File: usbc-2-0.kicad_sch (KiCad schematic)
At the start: 8 parts, among them J201 USB_C_Receptacle_USB2.0

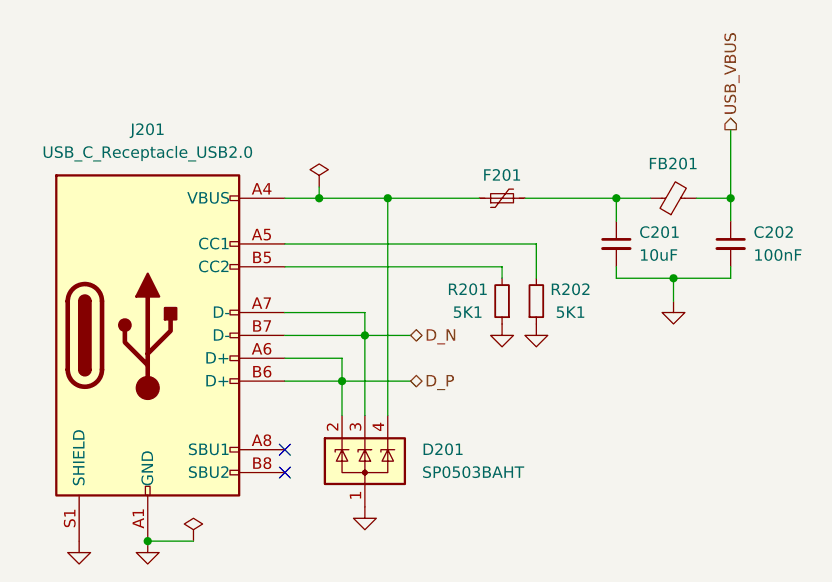
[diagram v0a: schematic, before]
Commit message: update schematic
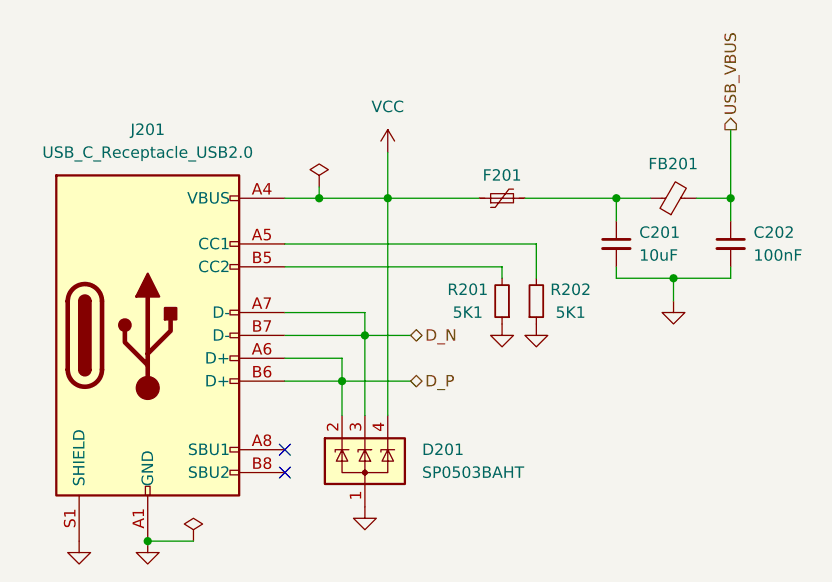
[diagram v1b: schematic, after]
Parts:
- J201: footprint User Custom Footprint:USB_C_Receptable_918-418K2023S40001 -> User_Footprint:USB_C_Receptable_918-418K2023S40001
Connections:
- net VCC: now reaches D201.4 (K), F201.1, J201.A4 (VBUS), J201.A9 (VBUS), J201.B4 (VBUS), J201.B9 (VBUS)
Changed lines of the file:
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@@
+    (stroke (width 0) (type default))
+  )
+  (wire (pts (xy 77.47 33.02) (xy 77.47 38.1))
     (stroke (width 0) (type default))
   )
@@
   (symbol (lib_id "power:GND") (at 90.17 52.07 0) (unit 1)
     (in_bom yes) (on_board yes) (dnp no) (fields_autoplaced)
-    (property "Reference" "#PWR0202" (at 90.17 58.42 0)
+    (property "Reference" "#PWR0203" (at 90.17 58.42 0)
       (effects (font (size 1.27 1.27)) hide)
     )
@@
       (project "wled-esp32-control-board"
         (path "/39949f26-7b4e-4f4c-975a-4ef261468b2a/06531422-46ec-4b81-b2a2-21a1afed1c45"
-          (reference "#PWR0202") (unit 1)
+          (reference "#PWR0203") (unit 1)
         )
       )
@@
   (symbol (lib_id "power:GND") (at 43.18 76.2 0) (unit 1)
     (in_bom yes) (on_board yes) (dnp no) (fields_autoplaced)
-    (property "Reference" "#PWR0205" (at 43.18 82.55 0)
+    (property "Reference" "#PWR0206" (at 43.18 82.55 0)
       (effects (font (size 1.27 1.27)) hide)
     )
@@
       (project "wled-esp32-control-board"
         (path "/39949f26-7b4e-4f4c-975a-4ef261468b2a/06531422-46ec-4b81-b2a2-21a1afed1c45"
+          (reference "#PWR0206") (unit 1)
+        )
+      )
+      (project "arudino-clone"
+        (path "/7b2b1845-59f7-4bfa-9efc-3639d821cf70"
+          (reference "#PWR?") (unit 1)
+        )
+        (path "/7b2b1845-59f7-4bfa-9efc-3639d821cf70/42f81444-0f87-48cc-869b-f9c5fa4e11c4"
           (reference "#PWR0205") (unit 1)
         )
       )
-      (project "arudino-clone"
-        (path "/7b2b1845-59f7-4bfa-9efc-3639d821cf70"
-          (reference "#PWR?") (unit 1)
-        )
-        (path "/7b2b1845-59f7-4bfa-9efc-3639d821cf70/42f81444-0f87-48cc-869b-f9c5fa4e11c4"
-          (reference "#PWR0205") (unit 1)
-        )
-      )
     )
   )
@@
       (effects (font (size 1.27 1.27)))
     )
-    (property "Footprint" "User Custom Footprint:USB_C_Receptable_918-418K2023S40001" (at 54.61 53.34 0)
+    (property "Footprint" "User_Footprint:USB_C_Receptable_918-418K2023S40001" (at 54.61 53.34 0)
       (effects (font (size 1.27 1.27)) hide)
     )
@@
     )
   )
+  (symbol (lib_id "power:VCC") (at 77.47 33.02 0) (unit 1)
+    (in_bom yes) (on_board yes) (dnp no) (fields_autoplaced)
+    (property "Reference" "#PWR0201" (at 77.47 36.83 0)
+      (effects (font (size 1.27 1.27)) hide)
+    )
+    (property "Value" "VCC" (at 77.47 27.94 0)
+      (effects (font (size 1.27 1.27)))
+    )
+    (property "Footprint" "" (at 77.47 33.02 0)
+      (effects (font (size 1.27 1.27)) hide)
+    )
+    (property "Datasheet" "" (at 77.47 33.02 0)
+      (effects (font (size 1.27 1.27)) hide)
+    )
+    (pin "1")
+    (instances
+      (project "wled-esp32-control-board"
+        (path "/39949f26-7b4e-4f4c-975a-4ef261468b2a/06531422-46ec-4b81-b2a2-21a1afed1c45"
+          (reference "#PWR0201") (unit 1)
+        )
+      )
+    )
+  )
   (symbol (lib_id "Device:R_Small") (at 90.17 49.53 180) (unit 1)
     (in_bom yes) (on_board yes) (dnp no)
@@
   (symbol (lib_id "power:GND") (at 50.8 76.2 0) (unit 1)
     (in_bom yes) (on_board yes) (dnp no) (fields_autoplaced)
-    (property "Reference" "#PWR0206" (at 50.8 82.55 0)
+    (property "Reference" "#PWR0207" (at 50.8 82.55 0)
       (effects (font (size 1.27 1.27)) hide)
     )
@@
       (project "wled-esp32-control-board"
         (path "/39949f26-7b4e-4f4c-975a-4ef261468b2a/06531422-46ec-4b81-b2a2-21a1afed1c45"
+          (reference "#PWR0207") (unit 1)
+        )
+      )
+      (project "arudino-clone"
+        (path "/7b2b1845-59f7-4bfa-9efc-3639d821cf70"
+          (reference "#PWR?") (unit 1)
+        )
+        (path "/7b2b1845-59f7-4bfa-9efc-3639d821cf70/42f81444-0f87-48cc-869b-f9c5fa4e11c4"
           (reference "#PWR0206") (unit 1)
         )
       )
-      (project "arudino-clone"
-        (path "/7b2b1845-59f7-4bfa-9efc-3639d821cf70"
-          (reference "#PWR?") (unit 1)
-        )
-        (path "/7b2b1845-59f7-4bfa-9efc-3639d821cf70/42f81444-0f87-48cc-869b-f9c5fa4e11c4"
-          (reference "#PWR0206") (unit 1)
-        )
-      )
     )
   )
   (symbol (lib_id "power:GND") (at 93.98 52.07 0) (unit 1)
     (in_bom yes) (on_board yes) (dnp no) (fields_autoplaced)
-    (property "Reference" "#PWR0203" (at 93.98 58.42 0)
+    (property "Reference" "#PWR0204" (at 93.98 58.42 0)
       (effects (font (size 1.27 1.27)) hide)
     )
@@
       (project "wled-esp32-control-board"
         (path "/39949f26-7b4e-4f4c-975a-4ef261468b2a/06531422-46ec-4b81-b2a2-21a1afed1c45"
-          (reference "#PWR0203") (unit 1)
+          (reference "#PWR0204") (unit 1)
         )
       )
@@
   (symbol (lib_id "power:GND") (at 74.93 72.39 0) (unit 1)
     (in_bom yes) (on_board yes) (dnp no) (fields_autoplaced)
-    (property "Reference" "#PWR0204" (at 74.93 78.74 0)
+    (property "Reference" "#PWR0205" (at 74.93 78.74 0)
       (effects (font (size 1.27 1.27)) hide)
     )
@@
       (project "wled-esp32-control-board"
         (path "/39949f26-7b4e-4f4c-975a-4ef261468b2a/06531422-46ec-4b81-b2a2-21a1afed1c45"
+          (reference "#PWR0205") (unit 1)
+        )
+      )
+      (project "arudino-clone"
+        (path "/7b2b1845-59f7-4bfa-9efc-3639d821cf70"
+          (reference "#PWR?") (unit 1)
+        )
+        (path "/7b2b1845-59f7-4bfa-9efc-3639d821cf70/42f81444-0f87-48cc-869b-f9c5fa4e11c4"
           (reference "#PWR0204") (unit 1)
         )
       )
-      (project "arudino-clone"
-        (path "/7b2b1845-59f7-4bfa-9efc-3639d821cf70"
-          (reference "#PWR?") (unit 1)
-        )
-        (path "/7b2b1845-59f7-4bfa-9efc-3639d821cf70/42f81444-0f87-48cc-869b-f9c5fa4e11c4"
-          (reference "#PWR0204") (unit 1)
-        )
-      )
     )
   )
@@
   (symbol (lib_id "power:GND") (at 109.22 49.53 0) (unit 1)
     (in_bom yes) (on_board yes) (dnp no) (fields_autoplaced)
-    (property "Reference" "#PWR0201" (at 109.22 55.88 0)
+    (property "Reference" "#PWR0202" (at 109.22 55.88 0)
       (effects (font (size 1.27 1.27)) hide)
     )
@@
       (project "wled-esp32-control-board"
         (path "/39949f26-7b4e-4f4c-975a-4ef261468b2a/06531422-46ec-4b81-b2a2-21a1afed1c45"
-          (reference "#PWR0201") (unit 1)
-        )
-      )
+          (reference "#PWR0202") (unit 1)
+        )
+      )

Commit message: update parts
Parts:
- J201: Mouser (none) -> 523-12402012E212A
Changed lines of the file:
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@@
+      (effects (font (size 1.27 1.27)) hide)
+    )
+    (property "Mouser" "523-12402012E212A" (at 50.8 53.34 0)
       (effects (font (size 1.27 1.27)) hide)
     )

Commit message: add mouser part numbers
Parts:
- C201: Mouser (none) -> 581-0805ZD106K
- C202: Mouser (none) -> 581-06035C104KAT2A
- D201: Mouser (none) -> 576-SP0503BAHTG
- F201: Mouser (none) -> 576-0603L200SL-VYR
- FB201: Mouser (none) -> 810-MPZ2012S101AT000
- R201, R202: Mouser (none) -> 603-RC0603FR-075K1L
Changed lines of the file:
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@@
+      (effects (font (size 1.27 1.27)) hide)
+    )
+    (property "Mouser" "576-SP0503BAHTG" (at 74.93 67.31 0)
       (effects (font (size 1.27 1.27)) hide)
     )
@@
       (effects (font (size 1.27 1.27)) hide)
     )
+    (property "Mouser" "581-06035C104KAT2A" (at 115.57 43.18 0)
+      (effects (font (size 1.27 1.27)) hide)
+    )
     (pin "1")
     (pin "2")
@@
     )
     (property "LCSC" "C74487" (at 109.22 38.1 0)
+      (effects (font (size 1.27 1.27)) hide)
+    )
+    (property "Mouser" "810-MPZ2012S101AT000" (at 109.22 38.1 0)
       (effects (font (size 1.27 1.27)) hide)
     )
@@
       (effects (font (size 1.27 1.27)) hide)
     )
+    (property "Mouser" "603-RC0603FR-075K1L" (at 90.17 49.53 0)
+      (effects (font (size 1.27 1.27)) hide)
+    )
     (pin "1")
     (pin "2")
@@
     )
     (property "LCSC" "C23186" (at 93.98 49.53 0)
+      (effects (font (size 1.27 1.27)) hide)
+    )
+    (property "Mouser" "603-RC0603FR-075K1L" (at 93.98 49.53 0)
       (effects (font (size 1.27 1.27)) hide)
     )
@@
       (effects (font (size 1.27 1.27)) hide)
     )
+    (property "Mouser" "581-0805ZD106K" (at 102.87 43.18 0)
+      (effects (font (size 1.27 1.27)) hide)
+    )
     (pin "1")
     (pin "2")
@@
       (effects (font (size 1.27 1.27)) hide)
     )
+    (property "Mouser" "576-0603L200SL-VYR" (at 90.17 38.1 0)
+      (effects (font (size 1.27 1.27)) hide)
+    )

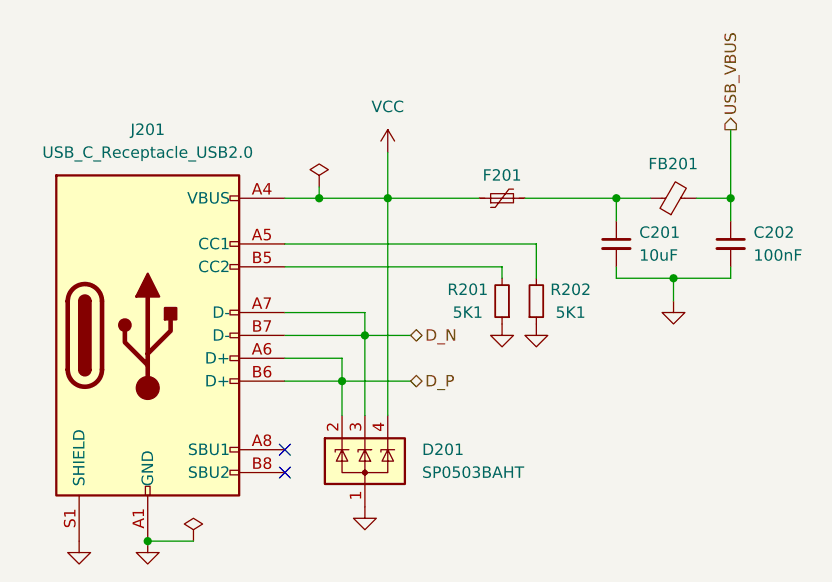
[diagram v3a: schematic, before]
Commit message: update design to replace CP2102 and LDO
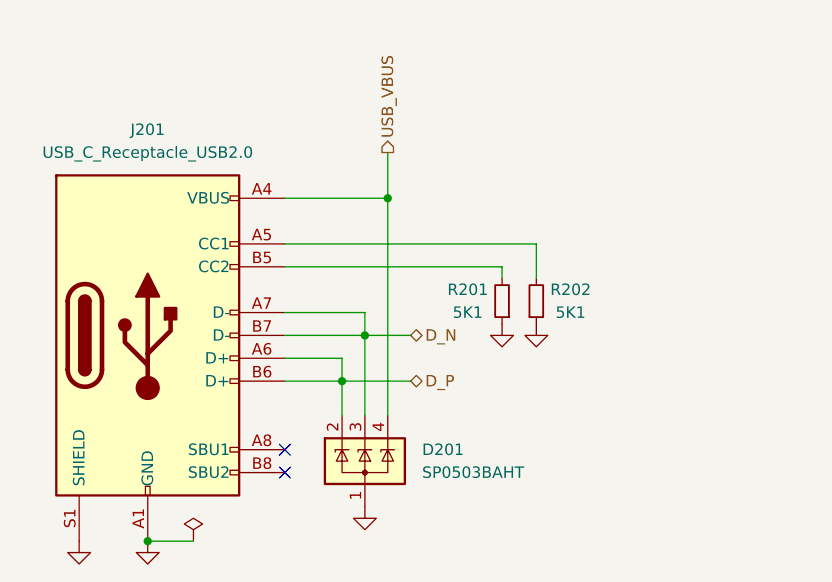
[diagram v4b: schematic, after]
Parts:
- removed C201: 10uF, Capacitor_SMD:C_0805_2012Metric, symbol Device:C_Small
- removed C202: 100nF, Capacitor_SMD:C_0603_1608Metric, symbol Device:C_Small
- removed F201: Polyfuse_Small, Fuse:Fuse_0603_1608Metric, symbol Device:Polyfuse_Small
- removed FB201: FerriteBead_Small, Resistor_SMD:R_0805_2012Metric, symbol Device:FerriteBead_Small
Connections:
- net VCC is gone; now on net USB_VBUS: D201.4 (K), J201.A4 (VBUS), J201.A9 (VBUS), J201.B4 (VBUS), J201.B9 (VBUS)
